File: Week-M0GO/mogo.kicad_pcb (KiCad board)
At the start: 2 copper layers, 31 parts, among them J1 USB_OTG, J2 Conn_01x06_Female, J3 Conn_01x20_Female, J4 Conn_01x20_Female, Q1 Q_PMOS_GDS, U1 CAT24C256, U2 STM32F072C8Tx, U3 AP7333-33SRG-7, Y1 Crystal 8Mhz, Y2 Crystal 32.76 Khz

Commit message: started routing
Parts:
- added SW1: SW_Push, Button_Switch_SMD:SW_SPST_TL3342, F.Cu at (93.4, 156.4)
- BT1: footprint Battery_Holders:Keystone_1058_1x2032-CoinCell -> Battery:BatteryHolder_Keystone_3000_1x12mm; moved to B.Cu
- J2: footprint Pin_Headers:Pin_Header_Straight_1x05_Pitch2.54mm -> Connector_PinHeader_2.54mm:PinHeader_1x06_P2.54mm_Vertical
- moved Y1 117.4 mm to (72.8, 187.6)
- moved J2 114.4 mm to (76.2, 149.9), turned to 90 degrees
- moved J1 109.7 mm to (82.8, 161.4)
- moved R1 98.1 mm to (85.5, 188.5)
- moved R8 98.1 mm to (88.0, 188.5)
- moved C8 96.8 mm to (70.2, 179.5)
- moved C1 96.8 mm to (73.0, 175.6)
- moved C3 96.8 mm to (73.0, 176.9)
- moved C4 96.8 mm to (75.9, 176.8)
- moved C5 96.8 mm to (78.7, 176.8)
- moved C9 96.8 mm to (70.2, 175.6)
- moved D1 96.8 mm to (76.2, 175.2)
- moved D2 96.8 mm to (79.4, 175.2)
- moved U1 96.8 mm to (78.3, 171.5)
- moved C2 96.8 mm to (70.2, 176.9)
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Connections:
- J3 pad 9: /PB3 -> /PB4
- U2 pad 40: /PB3 -> /PB4
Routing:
- net /PB15: track 0.00 -> 44.8 mm
- net /PB14: track 0.00 -> 42.6 mm
- net /PB11: track 0.00 -> 40.8 mm, vias 0 -> 3
- net /PB13: track 0.00 -> 40.3 mm
- net /PB12: track 0.00 -> 38.0 mm
- net /PB10: track 0.00 -> 36.7 mm, vias 0 -> 2
- net /PA8: track 0.00 -> 31.0 mm
- net /PB0: track 0.00 -> 29.8 mm
- net /PC13: track 0.00 -> 29.8 mm
- net /PB1: track 0.00 -> 29.2 mm
- net /PA9: track 0.00 -> 28.5 mm, vias 0 -> 1
- net /PB2: track 0.00 -> 28.5 mm
- net /RTC_OSC_IN: track 0.00 -> 26.7 mm
- net /RTC_OSC_OUT: track 0.00 -> 24.4 mm
- net /PB9: track 0.00 -> 22.8 mm
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
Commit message: board work m0go
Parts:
- Y1: value Crystal 8Mhz -> Crystal_GND24; footprint Crystals:Crystal_SMD_3225-4pin_3.2x2.5mm -> Crystal:Crystal_SMD_SeikoEpson_FA238-4Pin_3.2x2.5mm
- moved R8 64.3 mm to (87.8, 124.2)
- moved R1 58.9 mm to (77.7, 130.0), turned to 135 degrees
- moved Y1 55.2 mm to (75.9, 132.5), turned to 225 degrees
- moved D2 53.5 mm to (81.7, 121.7), turned to 135 degrees
- moved R2 53.4 mm to (76.5, 135.6), turned to 225 degrees
- moved C4 52.0 mm to (78.2, 124.8), turned to 45 degrees
- moved Y2 51.1 mm to (78.4, 128.0), turned to 45 degrees
- moved C3 50.1 mm to (76.2, 126.9), turned to 225 degrees
- moved C6 49.1 mm to (83.8, 132.4), turned to 45 degrees
- moved C8 48.4 mm to (84.7, 133.3), turned to 45 degrees
- moved SW1 46.0 mm to (81.4, 112.0), turned to 180 degrees
- moved C5 45.5 mm to (83.0, 131.5), turned to 45 degrees
- moved C1 45.0 mm to (74.1, 130.6), turned to 225 degrees
- moved C2 42.7 mm to (73.6, 134.3), turned to 135 degrees
- moved R6 41.8 mm to (81.6, 128.9), turned to 135 degrees
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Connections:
- J3 pad 1: +BATT -> /PB15
- J3 pad 10: /PB5 -> /PB3
- J3 pad 11: /PB6 -> /PB4
- J3 pad 12: /PB7 -> /PB5
- J3 pad 13: /PB8 -> /PB6
- J3 pad 14: /PB9 -> /PB7
- J3 pad 15: /PB10 -> /PB8
- J3 pad 16: /PB11 -> /PB9
- J3 pad 17: /PB12 -> +BATT
- J3 pad 18: /PB13 -> /_RESET
- J3 pad 19: /PB14 -> /BOOT0
- J3 pad 2: /_RESET -> /PA8
- J3 pad 20: /PB15 -> VBUS
- J3 pad 3: /BOOT0 -> /PA9
- J3 pad 4: VBUS -> /PA10
- J3 pad 5: /PB0 -> /USB_D-
- J3 pad 6: /PB1 -> /USB_D+
- J3 pad 7: /PB2 -> /SWDIO
- J3 pad 8: /PB3 -> /SWCLK
- J3 pad 9: /PB4 -> /PA15
- J4 pad 13: /PA8 -> /PB0
- J4 pad 14: /PA9 -> /PB1
- J4 pad 15: /PA10 -> /PB2
- J4 pad 16: /USB_D- -> /PB10
- J4 pad 17: /USB_D+ -> /PB11
- J4 pad 18: /SWDIO -> /PB12
- J4 pad 19: /SWCLK -> /PB13
- J4 pad 20: /PA15 -> /PB14
- Y1 pad 2: Net-(C2-Pad1) -> GND
- Y1 pad 3: (no net) -> Net-(C2-Pad1)
- Y1 pad 4: (no net) -> GND
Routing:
- net /USB_D-: track 0.00 -> 38.5 mm, vias 0 -> 1
- net /USB_D+: track 0.00 -> 36.1 mm, vias 0 -> 1
- net /SWCLK: track 0.00 -> 31.2 mm, vias 0 -> 1
- net /PB11: track 40.8 -> 13.8 mm, vias 3 -> 0
- net /PC13: track 29.8 -> 55.2 mm, vias 0 -> 1
- net /SWDIO: track 3.59 -> 27.3 mm, vias 0 -> 1
- net /PB10: track 36.7 -> 14.8 mm, vias 2 -> 0
- net /PB15: track 44.8 -> 23.2 mm
- net /RTC_OSC_IN: track 26.7 -> 6.02 mm
- net /PB12: track 38.0 -> 18.5 mm
- net /PB13: track 40.3 -> 21.5 mm
- net /PB0: track 29.8 -> 11.1 mm
- net /PB1: track 29.2 -> 10.6 mm
- net +3V3: track 0.00 -> 17.7 mm, vias 0 -> 3
- net /PB14: track 42.6 -> 25.4 mm
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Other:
- board outline added: 29.5 x 61.5 mm
- net class JLCPCB5mil added: clearance 0.127, trace_width 0.127, via_dia 0.6, via_drill 0.3
- net class PowerTrace added: clearance 0.254, trace_width 0.254, via_dia 0.8, via_drill 0.4
- rule trace_min: 0.2 -> 0.127
- rule via_min_size: 0.4 -> 0.6

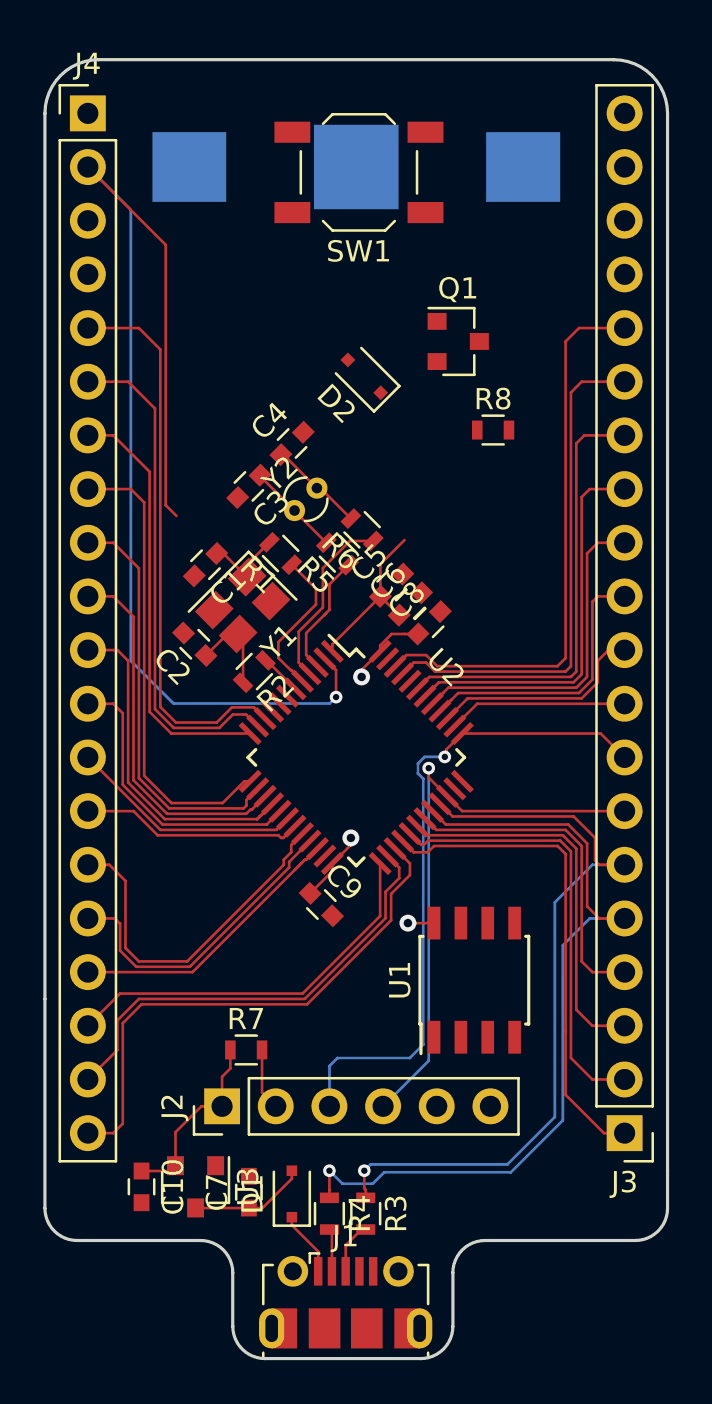
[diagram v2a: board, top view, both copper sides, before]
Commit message: mogo routing finished
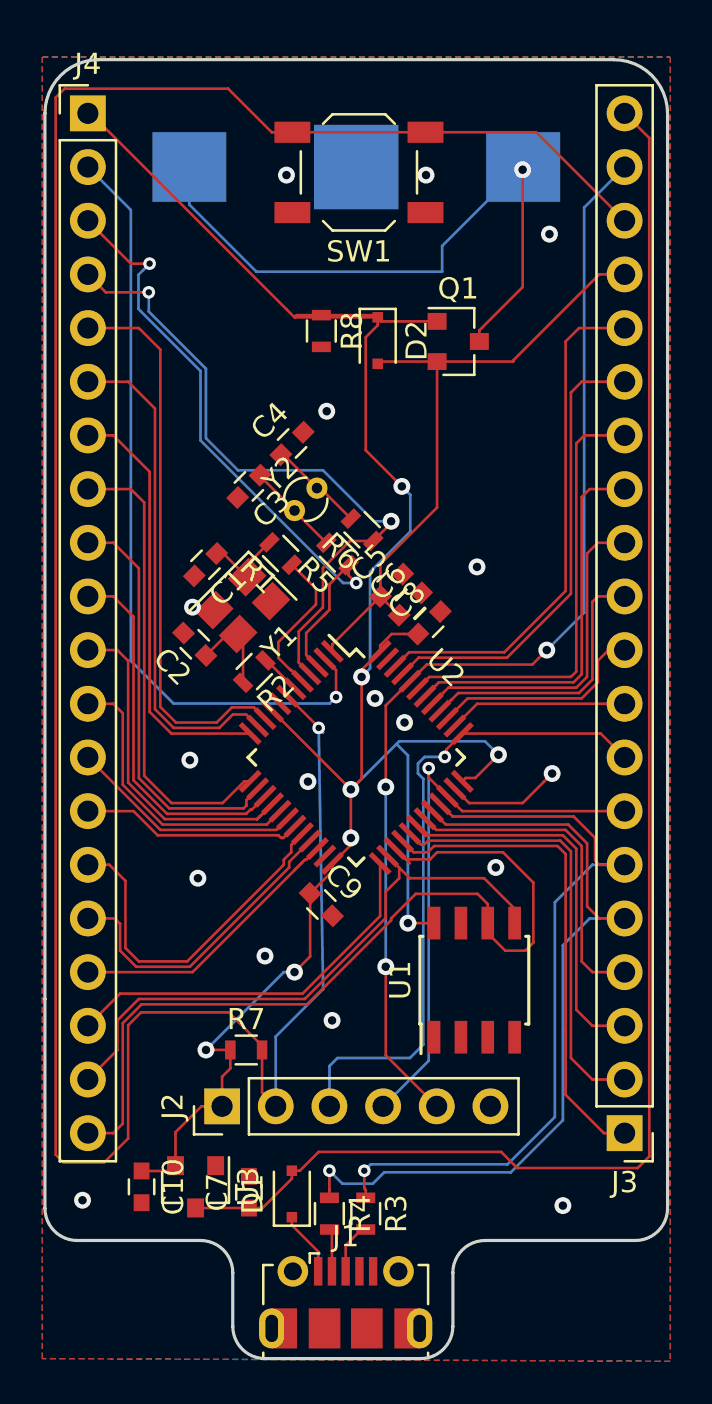
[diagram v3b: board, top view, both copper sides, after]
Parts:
- moved R8 9.38 mm to (79.6, 119.5), turned to 270 degrees
- moved D2 1.81 mm to (82.3, 120.0), turned to 270 degrees
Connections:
- U1 pad 5: /SDA_3V3 -> /PB13
- U1 pad 6: /SCL_3V3 -> /PB14
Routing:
- net /_RESET: track 2.93 -> 121.0 mm, vias 0 -> 1
- net +3V3: track 17.7 -> 104.5 mm, vias 3 -> 8
- net VBUS: track 5.51 -> 73.2 mm
- net /BOOT0: track 0.00 -> 53.1 mm, vias 0 -> 3
- net Net-(BT1-Pad1): track 0.00 -> 30.6 mm, vias 0 -> 1
- net /RTC_OSC_IN: track 6.02 -> 30.7 mm, vias 0 -> 2
- net /RTC_OSC_OUT: track 8.61 -> 31.7 mm, vias 0 -> 2
- net +BATT: track 7.94 -> 30.5 mm
- net /PC13: track 55.2 -> 37.0 mm
- net /PB14: track 25.4 -> 42.0 mm
- net /PB13: track 21.5 -> 28.5 mm
- net GND: track 0.00 -> 5.46 mm, vias 0 -> 17
- net /PB8: track 24.2 -> 21.8 mm
- net /PB9: track 26.7 -> 24.4 mm
- added copper zone on B.Cu, net GND
- added copper zone on F.Cu, net GND

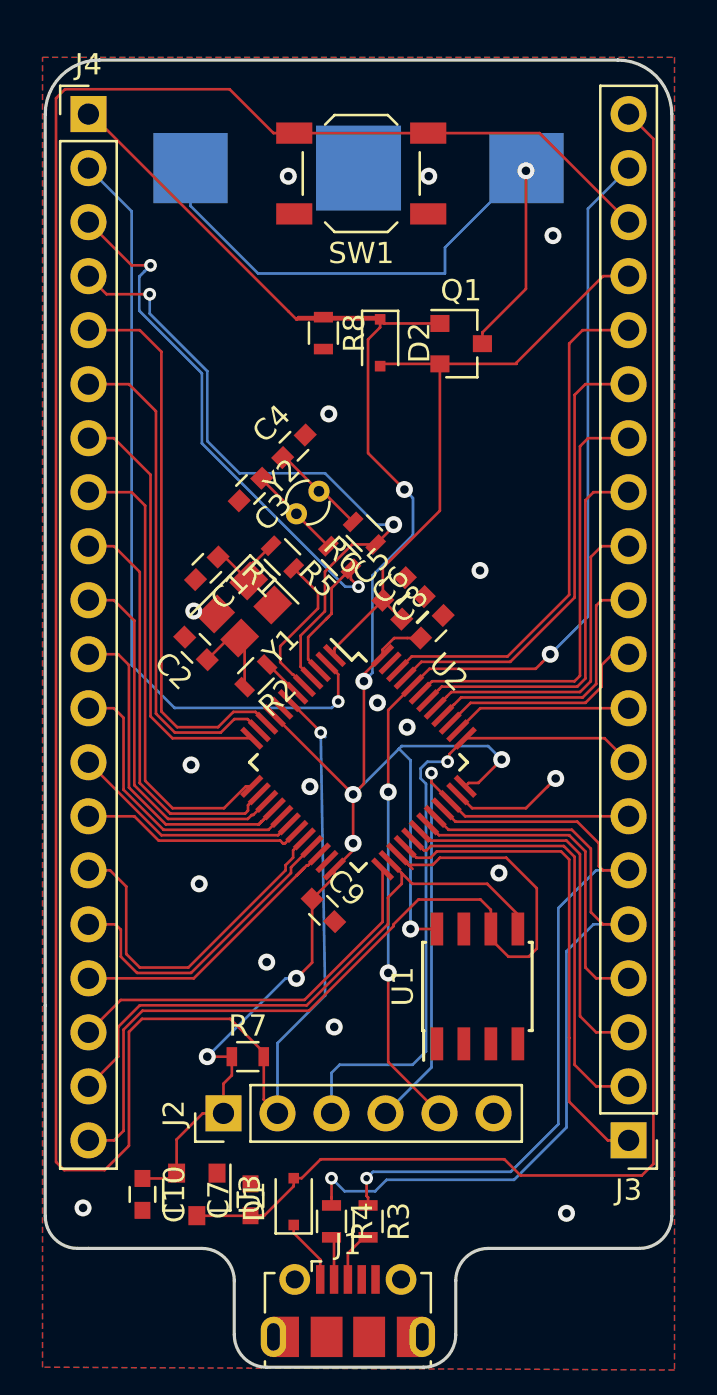
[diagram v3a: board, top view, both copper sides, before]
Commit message: routign finisted on M0GO
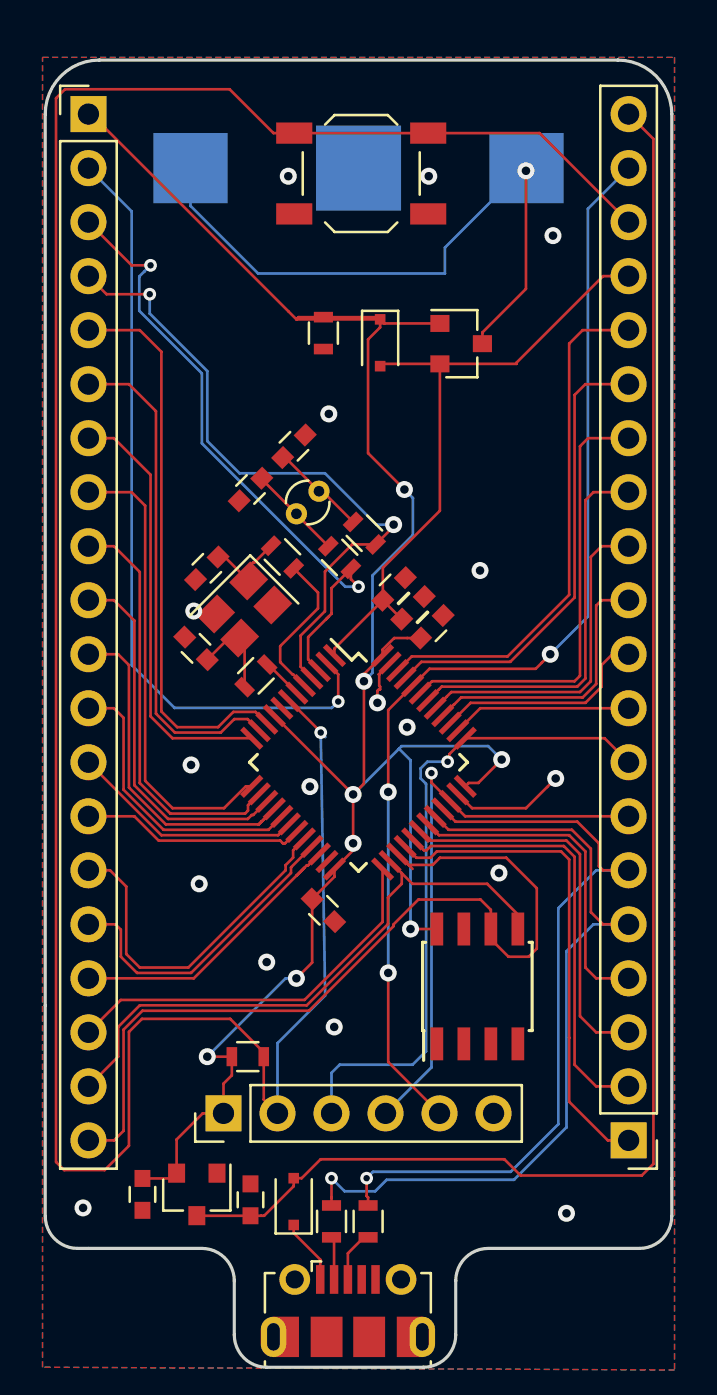
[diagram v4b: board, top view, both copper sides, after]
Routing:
- net GND: track 5.46 -> 7.67 mm
